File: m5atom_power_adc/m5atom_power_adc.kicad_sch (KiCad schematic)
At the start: 68 parts, among them J101 USB_C_Receptacle_USB2.0_16P, J102 Conn_01x04_Pin, J103 SubBatt, J104 MainBatt, J105 I2C, J106 Shunt, Q101 AO3401A, Q102 MMBT2222A, Q103 AO3401A, SW101 Boot, SW102 Reset, U101 LM2596S-5, U102 AMS1117-3.3, U103 ESP32-S3-MINI-1, U104 AMS1117-3.3, U105 LTC2944, U106 ADS1115IDGS

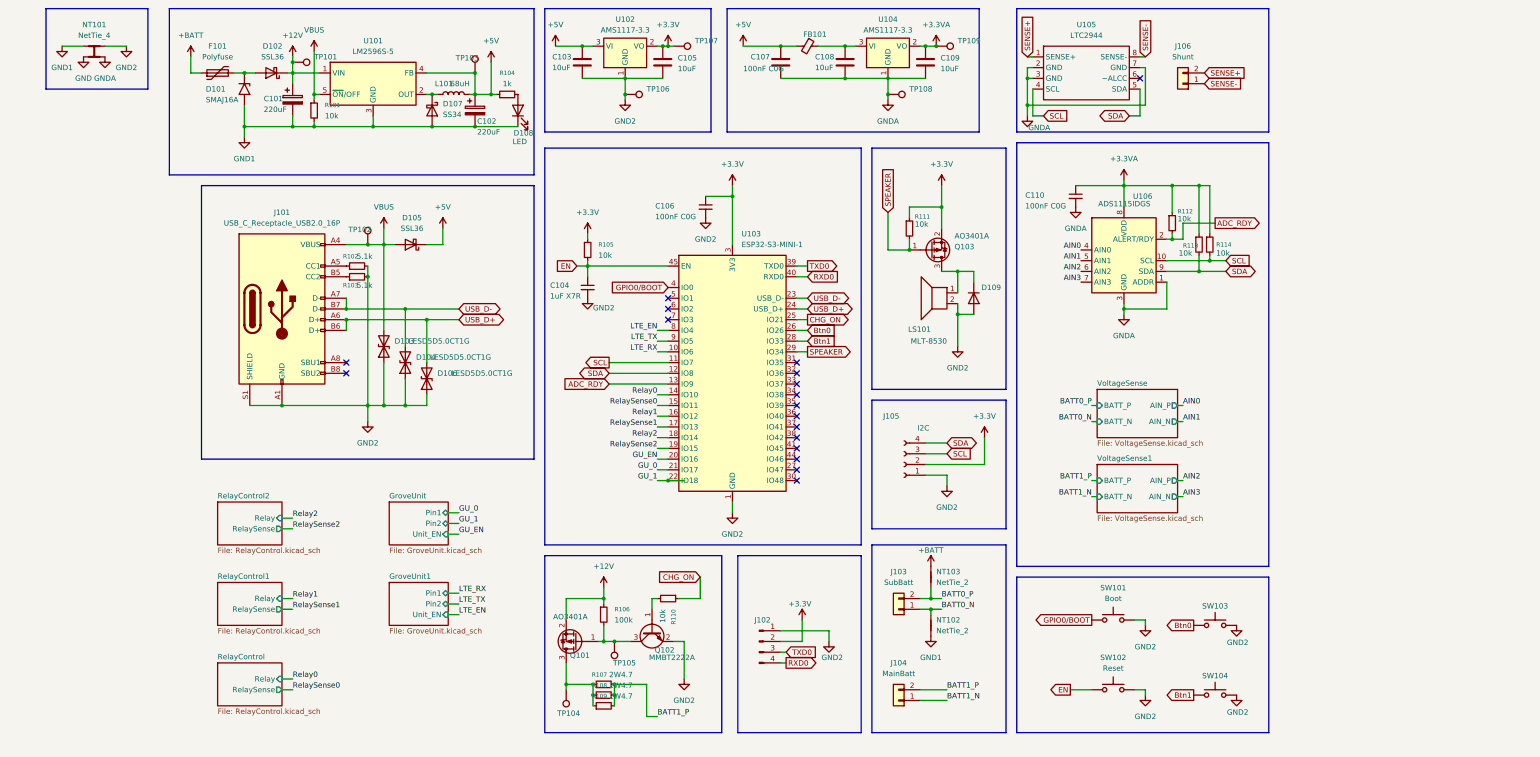
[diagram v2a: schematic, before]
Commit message: feat: PCBレイアウト完成・ドキュメントにサブシート構成を反映
- m5atom_power_adc: PCBレイアウト完成（80×82.5mm、131部品、ルーティング完了）
- GroveUnit/RelayControl サブシート更新
- CONTEXT.md/README.md: m5atom_power_adc のファイル構成にサブシート3枚・Library.pretty を追記

Co-Authored-By: Claude Sonnet 4.6 <noreply@anthropic.com>
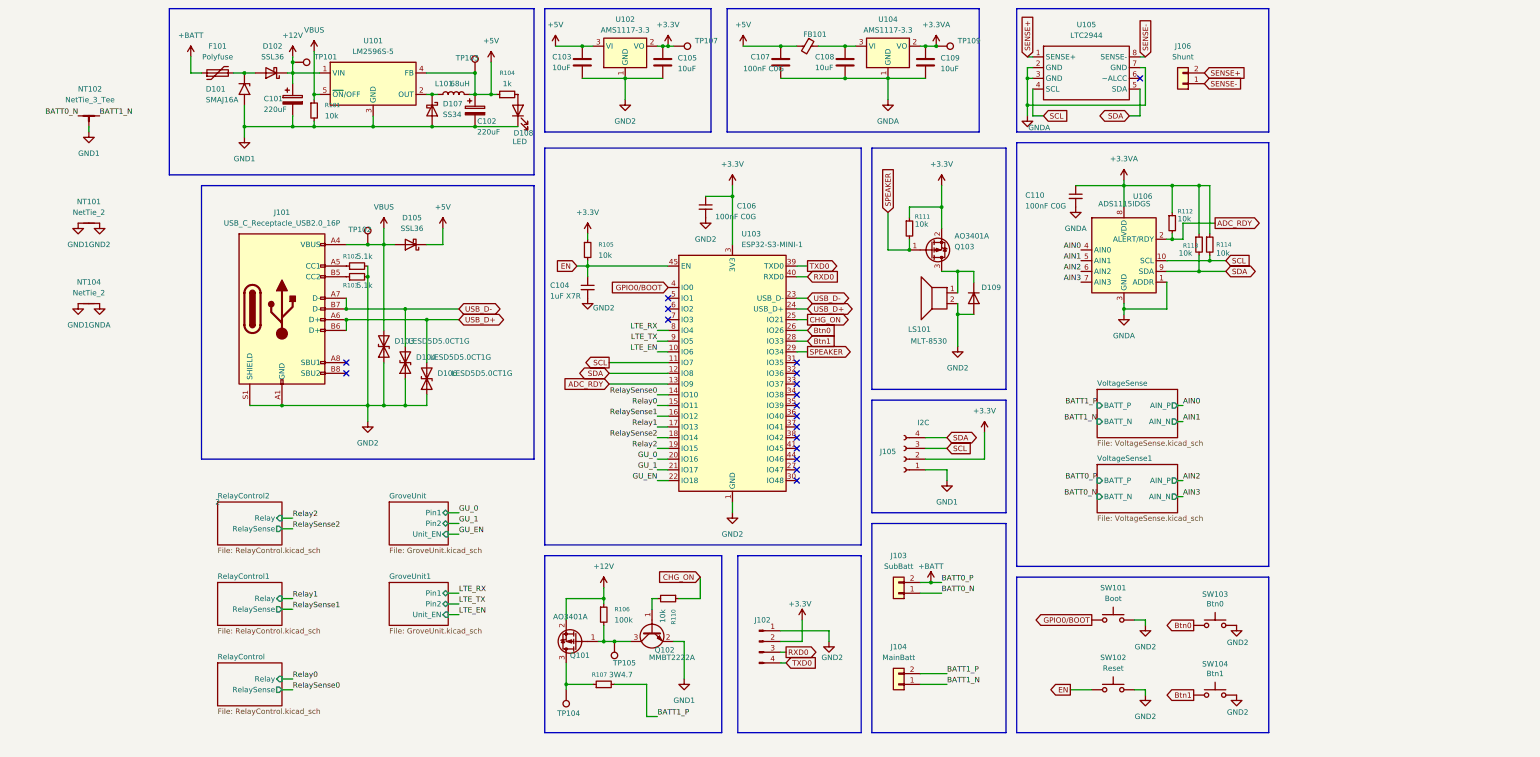
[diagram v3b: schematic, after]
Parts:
- removed NT101: NetTie_4, symbol Device:NetTie_4
- removed NT102, NT103: NetTie_2, symbol Device:NetTie_2
- removed R108, R109: 2W4.7, Resistor_SMD:R_2512_6332Metric, symbol Device:R_Small
- removed TP106, TP108: TestPoint, TestPoint:TestPoint_Pad_D1.5mm, symbol Connector:TestPoint
- added NT101: NetTie_2, NetTie:NetTie-2_SMD_Pad2.0mm, symbol Device:NetTie_2
- added NT102: NetTie_3_Tee, NetTie:NetTie-3_SMD_Pad2.0mm, symbol Device:NetTie_3_Tee
- added NT104: NetTie_2, NetTie:NetTie-2_SMD_Pad0.5mm, symbol Device:NetTie_2
- R107: value 2W4.7 -> 3W4.7; JLC_Num C876270 -> C3924519
- SW103: value ~ -> Btn0
- SW104: value ~ -> Btn1
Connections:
- net BATT0_P is gone; now on net +BATT: J103.2 (Pin_2)
- net BATT0_N: now also NT102.1
- net BATT1_N: now also NT102.2
- net GND1: now also J105.1 (Pin_1), Q102.2 (E), NT101.1, NT102.3, NT104.1
- net GND2: now also NT101.2; no longer J105.1 (Pin_1), Q102.2 (E)
- net GNDA: now also NT104.2
- net GU_0: now also U103.20 (IO16); no longer U103.21 (IO17)
- net GU_1: now also U103.21 (IO17); no longer U103.22 (IO18)
- net GU_EN: now also U103.22 (IO18); no longer U103.20 (IO16)
- net LTE_EN: now also U103.10 (IO6); no longer U103.8 (IO4)
- net LTE_RX: now also U103.8 (IO4); no longer U103.10 (IO6)
- net RXD0: now also J102.3 (Pin_3); no longer J102.4 (Pin_4)
- net Relay0: now also U103.15 (IO11); no longer U103.14 (IO10)
- net Relay1: now also U103.17 (IO13); no longer U103.16 (IO12)
- net Relay2: now also U103.19 (IO15); no longer U103.18 (IO14)
- net RelaySense0: now also U103.14 (IO10); no longer U103.15 (IO11)
- net RelaySense1: now also U103.16 (IO12); no longer U103.17 (IO13)
- net RelaySense2: now also U103.18 (IO14); no longer U103.19 (IO15)
- net TXD0: now also J102.4 (Pin_4); no longer J102.3 (Pin_3)
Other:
- moved on the sheet: J103, J104, J105

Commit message: chore: PCBレイアウト・回路図の細部修正
- GNDプレーン追加・整理（表裏、スターグラウンド構成）
- サーマルビア追加（ESP32、LM2596）
- 孤立GND島の除去
- 各種配線修正

Co-Authored-By: Claude Sonnet 4.6 <noreply@anthropic.com>
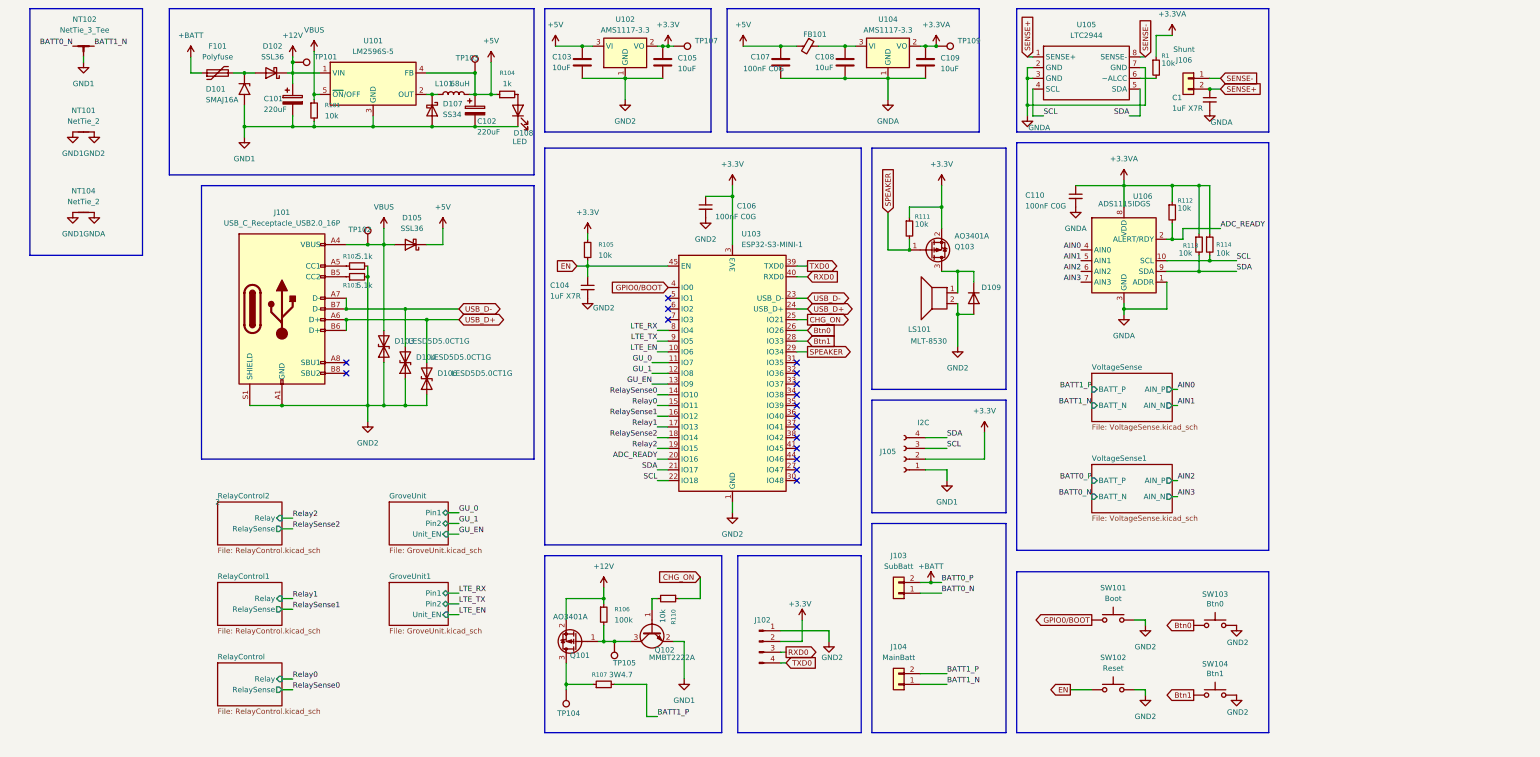
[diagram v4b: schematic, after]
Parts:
- added C1: 1uF X7R, Capacitor_SMD:C_0603_1608Metric, symbol Device:C_Small
- added R1: 10k, Resistor_SMD:R_0402_1005Metric, symbol Device:R_Small
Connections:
- net +3.3VA: now also R1.1
- net GNDA: now also C1.2
- net GU_0: now also U103.11 (IO7); no longer U103.20 (IO16)
- net GU_1: now also U103.12 (IO8); no longer U103.21 (IO17)
- net GU_EN: now also U103.13 (IO9); no longer U103.22 (IO18)
- net SCL: now also U103.22 (IO18); no longer U103.11 (IO7)
- net SDA: now also U103.21 (IO17); no longer U103.12 (IO8)
- net SENSE+: now also C1.1
- net at U105.6 (~ALCC): now also R1.2
- net ADC_RDY renamed ADC_READY
- net ADC_READY: now also U103.20 (IO16); no longer U103.13 (IO9)
- no-connect marks 18 -> 17
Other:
- moved on the sheet: J106, NT101, NT102, NT104, R112

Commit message: chore: PCBネジ穴追加・シルク整理・ロゴ追加・フットプリント修正
- ネジ穴を追加
- シルク文字・ロゴを整理・追加（k_icon フットプリント）
- HY2.0-4PZZ コネクタフットプリントを追加
- 各サブシートのフットプリント修正
- production/ を .gitignore に追加

Co-Authored-By: Claude Sonnet 4.6 <noreply@anthropic.com>
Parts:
- C101: JLC C125976 -> (none); JLC_Num C125976 -> (none); LCSC (none) -> C125976
- C102: JLC_Num C125976 -> (none); LCSC (none) -> C125976
- C103, C105, C108, C109: JLC_Num C32635 -> (none); LCSC (none) -> C32635
- C104: JLC_Num C5199872 -> (none); LCSC (none) -> C5199872
- C106, C107, C110: JLC_Num C2168319 -> (none); LCSC (none) -> C2168319
- C111: renamed from C1; JLC_Num C5199872 -> (none); LCSC (none) -> C5199872
- D101: JLC_Num C19077571 -> (none); LCSC (none) -> C19077571
- D102, D105: JLC_Num C28646286 -> (none); LCSC (none) -> C28646286
- D103, D104, D106: JLC_Num C5199850 -> (none); LCSC (none) -> C5199850
- D107: JLC_Num C8678 -> (none); LCSC (none) -> C8678
- D108: JLC_Num C965804 -> (none); LCSC (none) -> C965804
- D109: JLC_Num C2128 -> (none); LCSC (none) -> C2128
- F101: JLC_Num C18198333 -> (none); LCSC (none) -> C18198333
- FB101: JLC_Num C1017 -> (none); LCSC (none) -> C1017
- J101: JLC_Num C2765186 -> (none); LCSC (none) -> C2765186
- J103, J104, J106: JLC_Num C158012 -> (none); LCSC (none) -> C158012
- J105: footprint Connector_JST:JST_XH_S4B-XH-SM4-TB_1x04-1MP_P2.50mm_Horizontal -> Connector_JST:JST_XH_B4B-XH-A_1x04_P2.50mm_Vertical; JLC_Num C161861 -> (none); LCSC (none) -> C144395
- L101: JLC_Num C2983094 -> (none); LCSC (none) -> C2983094
- LS101: JLC_Num C94599 -> (none); LCSC (none) -> C94599
- Q101, Q103: JLC_Num C15127 -> (none); LCSC (none) -> C15127
- Q102: JLC_Num C8512 -> (none); LCSC (none) -> C8512
- R101, R105: JLC_Num C2906862 -> (none); LCSC (none) -> C2906862
- R102, R103: JLC_Num C2907045 -> (none); LCSC (none) -> C2907045
- R104: JLC_Num C21190 -> (none); LCSC (none) -> C21190
- R106: JLC_Num C2906981 -> (none); LCSC (none) -> C2906981
- R107: JLC_Num C3924519 -> (none); LCSC (none) -> C3924519
- R108: renamed from R110; JLC_Num C2906862 -> (none); LCSC (none) -> C2906862
- R109: renamed from R111; JLC_Num C2906862 -> (none); LCSC (none) -> C2906862
- R110: renamed from R1; JLC_Num C2906862 -> (none); LCSC (none) -> C2906862
- R111: renamed from R112; JLC_Num C2906862 -> (none); LCSC (none) -> C2906862
- R112: renamed from R113; JLC_Num C2906862 -> (none); LCSC (none) -> C2906862
- R113: renamed from R114; JLC_Num C2906862 -> (none); LCSC (none) -> C2906862
- SW101, SW102: JLC_Num C221897 -> (none); LCSC (none) -> C221897
- SW103, SW104: JLC_Num C221895 -> (none); LCSC (none) -> C221897
- TP101, TP102, TP103, TP104, TP105: now left out of the parts list
- TP106: renamed from TP107; now left out of the parts list
- TP107: renamed from TP109; now left out of the parts list
- U101: JLC_Num C5349985 -> (none); LCSC (none) -> C5349985
- U102, U104: JLC_Num C6186 -> (none); LCSC (none) -> C6186
- U103: JLC_Num C2913206 -> (none); LCSC (none) -> C2913206
- U105: JLC_Num C683672 -> (none); LCSC (none) -> C683672
- U106: footprint Package_SO:TSSOP-10_3x3mm_P0.5mm -> Package_SO:VSSOP-10_3x3mm_P0.5mm; JLC_Num C2651328 -> (none); LCSC (none) -> C468683
- renumbered NT102 to NT101, NT101 to NT102, NT104 to NT103

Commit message: chore: KiCadプロジェクト更新（回路図・PCBレイアウト各種修正）
Co-Authored-By: Claude Sonnet 4.6 <noreply@anthropic.com>
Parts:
- added C112: 100nF, Capacitor_SMD:C_0603_1608Metric, symbol Device:C_Small
- added U108: INA228, Package_SO:VSSOP-10_3x3mm_P0.5mm, symbol Sensor_Energy:INA228
- C111, R110, U105: now not fitted
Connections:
- net +3.3VA: now also C112.1, U108.6 (VS)
- net GNDA: now also C112.2, U108.1 (A1), U108.2 (A0), U108.7 (GND)
- net SCL: now also U108.5 (SCL)
- net SDA: now also U108.4 (SDA)
- net SENSE+: now also U108.10 (Vin+), U108.8 (Vbus)
- net SENSE-: now also U108.9 (Vin-)
- net INA_ALERT: now reaches U103.31 (IO35)
- net INA_ALERT: now also U108.3 (~{Alert})
- no-connect marks 17 -> 16
